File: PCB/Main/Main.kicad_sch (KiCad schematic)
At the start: 0 parts

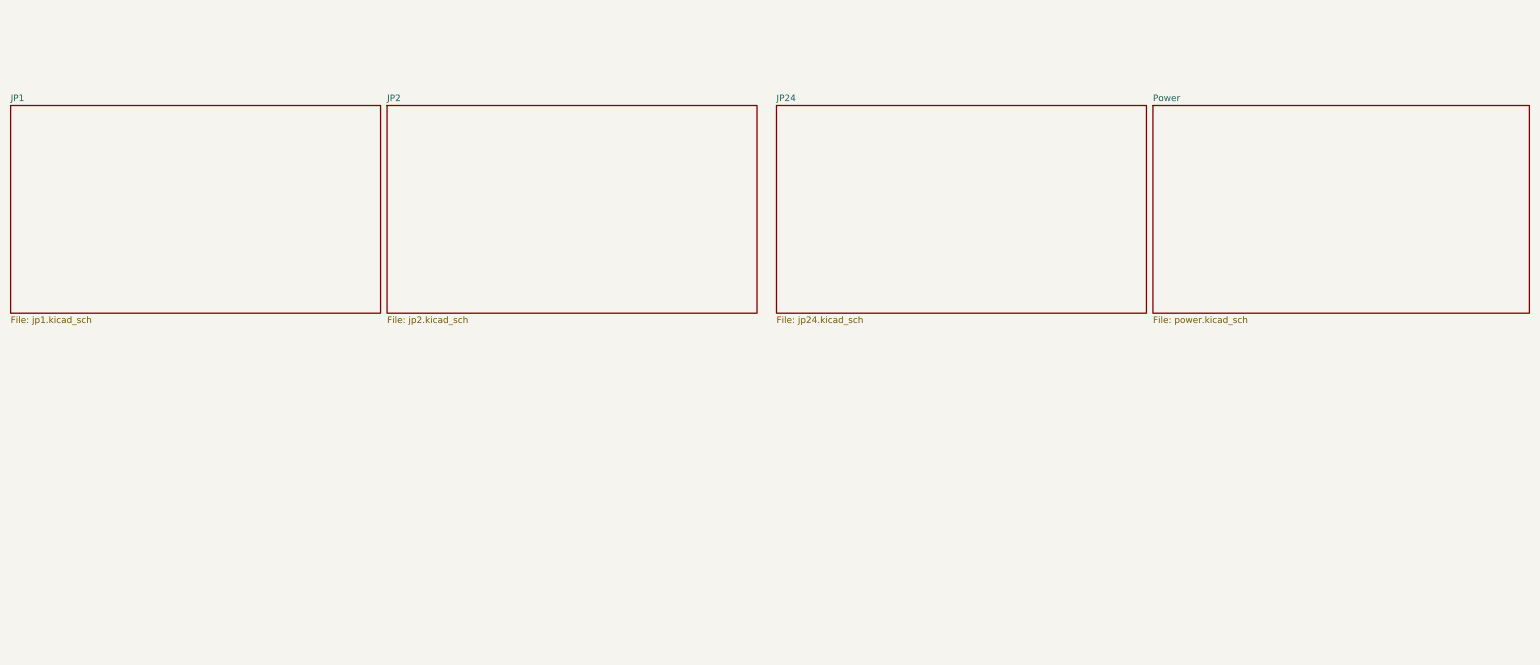
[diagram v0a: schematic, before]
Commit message: rename y conectores
tambien se añaden pours
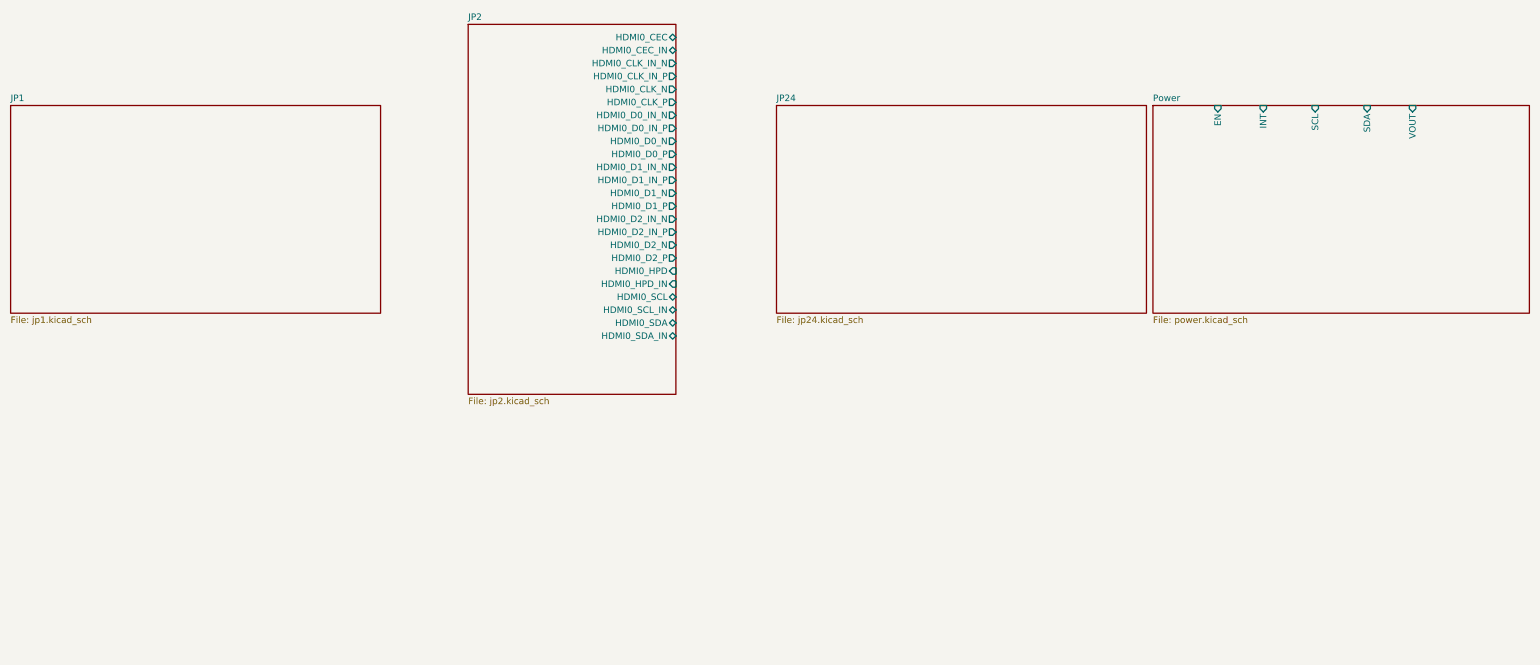
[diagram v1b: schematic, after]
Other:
- sheet JP2 ports: added HDMI0_CEC, HDMI0_CEC_IN, HDMI0_CLK_IN_N, HDMI0_CLK_IN_P, HDMI0_CLK_N, HDMI0_CLK_P, HDMI0_D0_IN_N, HDMI0_D0_IN_P, HDMI0_D0_N, HDMI0_D0_P, HDMI0_D1_IN_N, HDMI0_D1_IN_P, HDMI0_D1_N, HDMI0_D1_P, HDMI0_D2_IN_N, HDMI0_D2_IN_P, HDMI0_D2_N, HDMI0_D2_P, HDMI0_HPD, HDMI0_HPD_IN, HDMI0_SCL, HDMI0_SCL_IN, HDMI0_SDA, HDMI0_SDA_IN; removed none
- sheet Power ports: added EN, INT, SCL, SDA, VOUT; removed none

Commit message: pcb continued
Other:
- sheet JP1 ports: added EN; removed none
- sheet Power ports: added POWER_5V; removed VOUT
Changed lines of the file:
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@@
 	(generator_version "9.0")
 	(paper "A4")
+	(wire
+		(pts
+			(xy 236.22 212.09) (xy 8.89 212.09)
+		)
+		(stroke
+			(width 0)
+			(type default)
+		)
+	)
+	(wire
+		(pts
+			(xy 236.22 218.44) (xy 236.22 212.09)
+		)
+		(stroke
+			(width 0)
+			(type default)
+		)
+	)
+	(wire
+		(pts
+			(xy 8.89 212.09) (xy 8.89 218.44)
+		)
+		(stroke
+			(width 0)
+			(type default)
+		)
+	)
 	(sheet
-		(at 89.535 202.565)
+		(at 86.995 250.825)
 		(size 40.64 72.39)
 		(exclude_from_sim no)
@@
 		)
 		(property "Sheetname" "JP2"
-			(at 89.535 201.8534 0)
+			(at 86.995 250.1134 0)
 			(effects
 				(font
@@
 		)
 		(property "Sheetfile" "jp2.kicad_sch"
-			(at 89.535 275.5396 0)
+			(at 86.995 323.7996 0)
 			(effects
 				(font
@@
 		)
 		(pin "HDMI0_CEC" bidirectional
-			(at 130.175 205.105 0)
+			(at 127.635 253.365 0)
 			(effects
 				(font
@@
 		)
 		(pin "HDMI0_CEC_IN" bidirectional
-			(at 130.175 207.645 0)
+			(at 127.635 255.905 0)
 			(effects
 				(font
@@
 		)
 		(pin "HDMI0_CLK_IN_N" output
-			(at 130.175 210.185 0)
+			(at 127.635 258.445 0)
 			(effects
 				(font
@@
 		)
 		(pin "HDMI0_CLK_IN_P" output
-			(at 130.175 212.725 0)
+			(at 127.635 260.985 0)
 			(effects
 				(font
@@
 		)
 		(pin "HDMI0_CLK_N" output
-			(at 130.175 215.265 0)
+			(at 127.635 263.525 0)
 			(effects
 				(font
@@
 		)
 		(pin "HDMI0_CLK_P" output
-			(at 130.175 217.805 0)
+			(at 127.635 266.065 0)
 			(effects
 				(font
@@
 		)
 		(pin "HDMI0_D0_IN_N" output
-			(at 130.175 220.345 0)
+			(at 127.635 268.605 0)
 			(effects
 				(font
@@
 		)
 		(pin "HDMI0_D0_IN_P" output
-			(at 130.175 222.885 0)
+			(at 127.635 271.145 0)
 			(effects
 				(font
@@
 		)
 		(pin "HDMI0_D0_N" output
-			(at 130.175 225.425 0)
+			(at 127.635 273.685 0)
 			(effects
 				(font
@@
 		)
 		(pin "HDMI0_D0_P" output
-			(at 130.175 227.965 0)
+			(at 127.635 276.225 0)
 			(effects
 				(font
@@
 		)
 		(pin "HDMI0_D1_IN_N" output
-			(at 130.175 230.505 0)
+			(at 127.635 278.765 0)
 			(effects
 				(font
@@
 		)
 		(pin "HDMI0_D1_IN_P" output
-			(at 130.175 233.045 0)
+			(at 127.635 281.305 0)
 			(effects
 				(font
@@
 		)
 		(pin "HDMI0_D1_N" output
-			(at 130.175 235.585 0)
+			(at 127.635 283.845 0)
 			(effects
 				(font
@@
 		)
 		(pin "HDMI0_D1_P" output
-			(at 130.175 238.125 0)
+			(at 127.635 286.385 0)
 			(effects
 				(font
@@
 		)
 		(pin "HDMI0_D2_IN_N" output
-			(at 130.175 240.665 0)
+			(at 127.635 288.925 0)
 			(effects
 				(font
@@
 		)
 		(pin "HDMI0_D2_IN_P" output
-			(at 130.175 243.205 0)
+			(at 127.635 291.465 0)
 			(effects
 				(font
@@
 		)
 		(pin "HDMI0_D2_N" output
-			(at 130.175 245.745 0)
+			(at 127.635 294.005 0)
 			(effects
 				(font
@@
 		)
 		(pin "HDMI0_D2_P" output
-			(at 130.175 248.285 0)
+			(at 127.635 296.545 0)
 			(effects
 				(font
@@
 		)
 		(pin "HDMI0_HPD" input
-			(at 130.175 250.825 0)
+			(at 127.635 299.085 0)
 			(effects
 				(font
@@
 		)
 		(pin "HDMI0_HPD_IN" input
-			(at 130.175 253.365 0)
+			(at 127.635 301.625 0)
 			(effects
 				(font
@@
 		)
 		(pin "HDMI0_SCL" bidirectional
-			(at 130.175 255.905 0)
+			(at 127.635 304.165 0)
 			(effects
 				(font
@@
 		)
 		(pin "HDMI0_SCL_IN" bidirectional
-			(at 130.175 258.445 0)
+			(at 127.635 306.705 0)
 			(effects
 				(font
@@
 		)
 		(pin "HDMI0_SDA" bidirectional
-			(at 130.175 260.985 0)
+			(at 127.635 309.245 0)
 			(effects
 				(font
@@
 		)
 		(pin "HDMI0_SDA_IN" bidirectional
-			(at 130.175 263.525 0)
+			(at 127.635 311.785 0)
 			(effects
 				(font
@@
 			)
 		)
-		(pin "VOUT" input
-			(at 274.32 218.44 90)
+		(pin "POWER_5V" input
+			(at 273.05 218.44 90)
 			(effects
 				(font
@@
 			)
 		)
+		(pin "EN" output
+			(at 8.89 218.44 90)
+			(effects
+				(font
+					(size 1.27 1.27)
+				)
+				(justify right)
+			)
+		)
